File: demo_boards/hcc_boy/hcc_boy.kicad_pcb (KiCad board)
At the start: 2 copper layers, 18 x 22 mm, 24 parts, among them J2 TEST_1P, J4 TEST_1P, SW4 SW_PUSH, U1 MIC5353-3.3YMT-TR, U2 SAMD21G18, U4 SAMD21_MOD, Y1 Crystal_Small

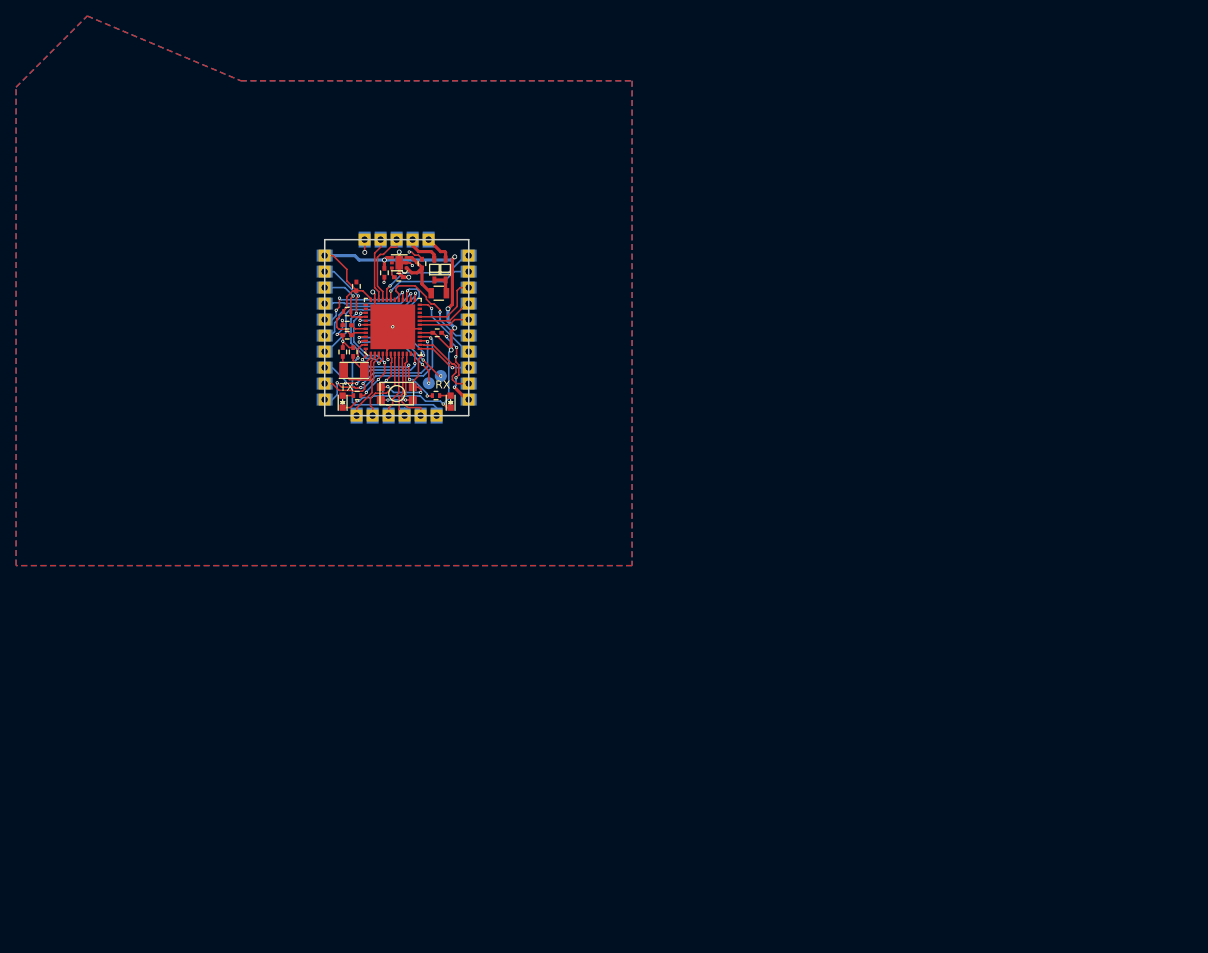
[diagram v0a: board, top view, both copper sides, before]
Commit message: added demo boards
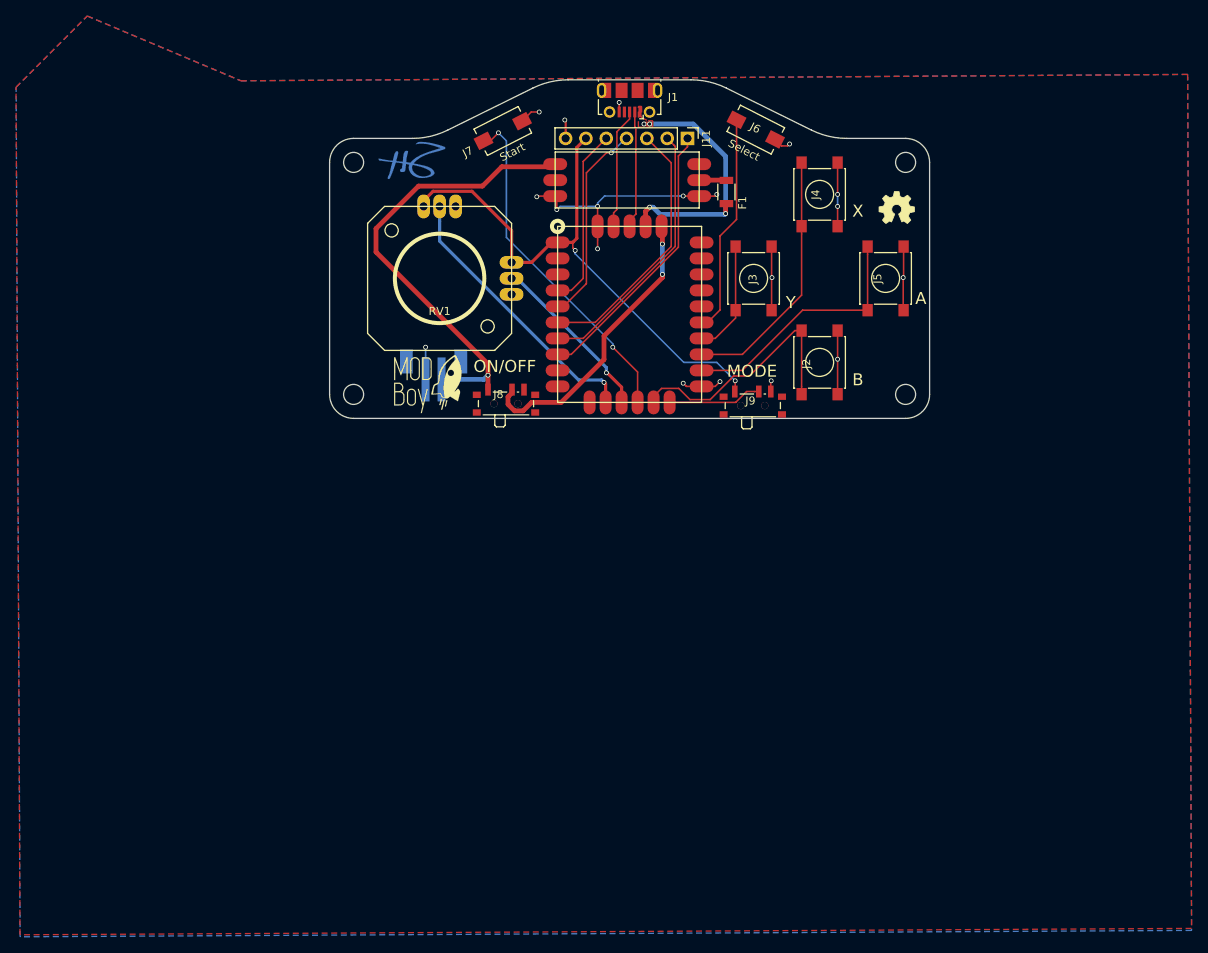
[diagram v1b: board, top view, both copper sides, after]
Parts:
- removed C11, C12, C3, C5, C6: 0.1uF, Capacitors_SMD:C_0402
- removed C2, C4: 15pF, Capacitors_SMD:C_0402
- removed C8, C9: 1uF, Capacitors_SMD:C_0402
- removed D1, D2: LED, LEDs:LED-0603
- removed D3, D4: BAT20J, agg:SOD-323
- removed R3: 10k, Resistors_SMD:R_0402
- removed R8, R9: 1k, Resistors_SMD:R_0402
- removed SW4: SW_PUSH, idlehands_footprints:switch_kmr2
- removed U2: SAMD21G18, idlehands_footprints:QFN-48-EP-ST_NoVia
- removed Y1: Crystal_Small, idlehands_footprints:crystal_smd_3.20x1.50mm2
- added BT1: Battery_Cell, Connectors_JST:JST_PH_B2B-PH-SM4-TB_02x2.00mm_Straight, B.Cu at (113.6, 94.3)
- added G***: LOGO, project_footprints:MODBoy_Logo, F.Cu at (113.0, 95.8)
- added G***: LOGO, project_footprints:MODBoy_Logo_Mask, F.Cu at (113.0, 95.8)
- added G***: LOGO, idlehands_footprints:SH_LOGO, B.Cu at (110.9, 68.2)
- added G***: LOGO, idlehands_footprints:SH_LOGOcu, B.Cu at (110.9, 68.2)
- added G***: LOGO, idlehands_footprints:OSHLogo, F.Cu at (171.5, 74.0)
- added J1: USB_OTG, Connectors_USB:USB_Micro-B_Molex-105017-0001, F.Cu at (138.1, 59.7)
- added J11: OLED, Pin_Headers:Pin_Header_Straight_1x07_Pitch2.54mm, F.Cu at (145.4, 65.3)
- added J3: B, project_footprints:SW_SPST_PTS645, F.Cu at (153.6, 82.8)
- added J5: Y, project_footprints:SW_SPST_PTS645, F.Cu at (170.1, 82.8)
- added J6: Start, Buttons_Switches_SMD:SW_SPST_EVQPE1, F.Cu at (153.9, 64.2)
- added J7: Select, Buttons_Switches_SMD:SW_SPST_EVQPE1, F.Cu at (122.3, 64.4)
- added J8: PWR, Buttons_Switches_SMD:SW_SPDT_PCM12, F.Cu at (122.7, 98.2)
- added J9: Selector, Buttons_Switches_SMD:SW_SPDT_PCM12, F.Cu at (153.5, 98.4)
- added RV1: JOYSTICK, idlehands_footprints:JOYSTICK_MINI_2AXIS, F.Cu at (114.4, 82.8)
- F1: value 500mA -> Fuse; footprint Resistors_SMD:R_0805 -> Resistors_SMD:R_1206
- J2: value TEST_1P -> A; footprint idlehands_footprints:TESTP_1_5 -> project_footprints:SW_SPST_PTS645; moved to F.Cu
- J4: value TEST_1P -> X; footprint idlehands_footprints:TESTP_1_5 -> project_footprints:SW_SPST_PTS645; moved to F.Cu
- U1: value MIC5353-3.3YMT-TR -> charge_mod; footprint agg:DFN-6-EP-ONSEMI -> idlehands_libs:LIPO_CHARGE_MOD_FOOTPRINT
- U4: footprint idlehands_footprints:SAMD21G18_MOD -> idlehands_libs:SAMD_HCC_G_FOOT
- moved J4 52.5 mm to (161.9, 72.3), turned to 90 degrees
- moved J2 48.9 mm to (161.9, 93.3), turned to 90 degrees
- moved F1 38.1 mm to (150.2, 72.0), turned to 90 degrees
- moved U1 30.3 mm to (137.8, 70.5), turned to 0 degrees
- moved U4 29.2 mm to (138.1, 87.3)
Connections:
- F1 pad 1: Net-(D3-Pad1) -> VBUS
- F1 pad 2: Net-(C8-Pad1) -> Net-(F1-Pad2)
- J2 pad 1: SWDIO -> A4
- J4 pad 1: SWCLK -> D4
- U1 pad 1: Net-(C8-Pad1) -> +BATT
- U1 pad 2: GND -> Net-(F1-Pad2)
- U1 pad 3: Net-(C8-Pad1) -> GND
- U4 pad 25: SDA -> SDI
- U4 pad 26: SCL -> CKI
- U4 pad 27: +BATT -> Net-(J8-Pad2)
- U4 pad 29: USB_D- -> Net-(J1-Pad2)
- U4 pad 30: USB_D+ -> Net-(J1-Pad3)
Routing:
- net +BATT: track 3.63 -> 57.7 mm, vias 0 -> 1
- net Net-(J8-Pad2): track 0.00 -> 36.8 mm, vias 0 -> 2
- net GND: track 48.9 -> 83.4 mm, vias 20 -> 19
- net A3: track 9.18 -> 43.2 mm, vias 0 -> 2
- net RESET: track 30.5 -> 0.00 mm, vias 5 -> 0
- net VBUS: track 4.49 -> 32.8 mm, vias 0 -> 4
- net D4: track 7.09 -> 32.1 mm, vias 1 -> 0
- net A1: track 9.90 -> 34.8 mm, vias 0 -> 1
- net D3: track 9.74 -> 31.8 mm
- net RX/D0: track 21.7 -> 0.00 mm, vias 3 -> 0
- net A4: track 10.8 -> 31.8 mm
- net D9: track 14.7 -> 34.7 mm, vias 3 -> 0
- net TX/D1: track 19.4 -> 0.00 mm, vias 2 -> 0
- net D11: track 15.5 -> 33.7 mm, vias 1 -> 0
- net AREF: track 17.7 -> 0.00 mm, vias 3 -> 0
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- added copper zone on F.Cu, net VBUS
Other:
- board size 18 x 22 mm -> 75 x 42.3 mm
- board text added: "A"
- board text added: "B"
- board text added: "MODBoy_V01p Kickstarter Demo Board for HCC MODULE YouTube.com/SeanHodginsFilms"
- board text added: "MODE"
- board text added: "ON/OFF"
- board text added: "Select"
- board text added: "Start"
- board text added: "X"
- board text added: "Y"
- board text removed: "RX"
- board text removed: "TX"
- board text removed: "bridge_mod v01p"

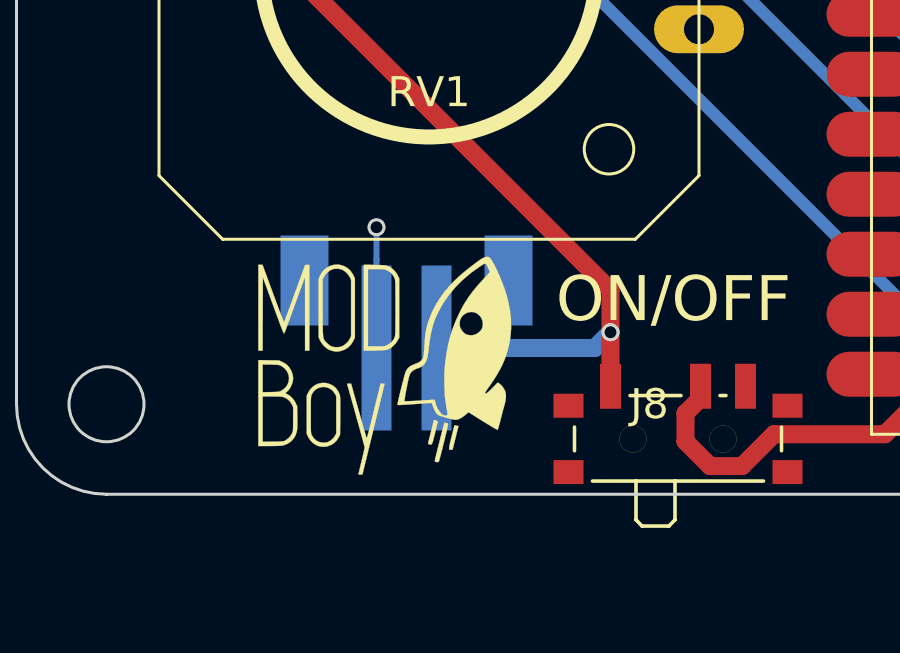
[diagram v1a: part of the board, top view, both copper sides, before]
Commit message: fixed battery connection on HCC_Boy
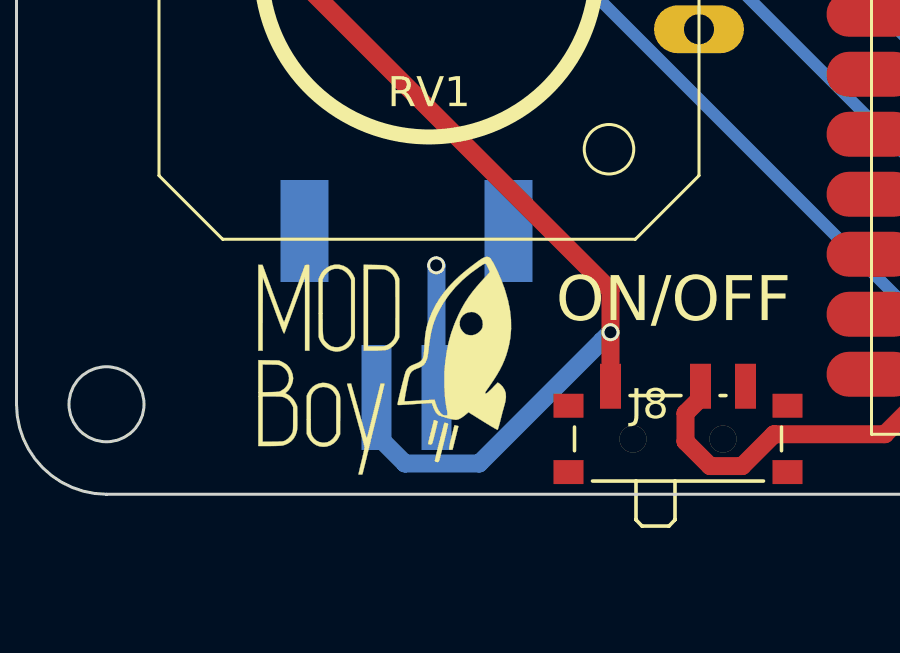
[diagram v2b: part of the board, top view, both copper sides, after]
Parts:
- BT1: footprint Connectors_JST:JST_PH_B2B-PH-SM4-TB_02x2.00mm_Straight -> Connectors_JST_PH:Connectors_JST_S2B-PH-SM4-TB
- turned BT1 to 0 degrees
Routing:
- net +BATT: track 57.7 -> 62.9 mm
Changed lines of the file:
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@@
-(kicad_pcb (version 4) (host pcbnew 4.0.4-stable)
+(kicad_pcb (version 4) (host pcbnew 4.0.7)
   (general
     (links 58)
-    (no_connects 7)
+    (no_connects 8)
     (area 61.42 50.05 208.370001 165.150001)
     (thickness 1.6)
     (drawings 36)
-    (tracks 237)
+    (tracks 240)
     (zones 0)
     (modules 20)
@@
   )
   (setup
-    (last_trace_width 0.2)
+    (last_trace_width 0.6)
     (user_trace_width 0.2)
     (user_trace_width 0.4)
@@
       (net 1 GND))
     (model ${KISYS3DMOD}/Pin_Headers.3dshapes/Pin_Header_Straight_1x07_Pitch2.54mm.wrl
-      (at (xyz 0 0 0))
-      (scale (xyz 1 1 1))
-      (rotate (xyz 0 0 0))
-    )
-  )
-  (module Connectors_JST:JST_PH_B2B-PH-SM4-TB_02x2.00mm_Straight (layer B.Cu)
-    (at 113.62 94.35 180)
-    (descr "JST PH series connector, B2B-PH-SM4-TB, top entry type, surface mount, Datasheet: http://www.jst-mfg.com/product/pdf/eng/ePH.pdf")
-    (tags "connector jst ph")
-    (attr smd)
-    (fp_text reference BT1 (at 0 4.625 180) (layer B.SilkS)
-      (effects (font (size 1 1) (thickness 0.15)) (justify mirror))
-    )
-    (fp_text value Battery_Cell (at 0 -4.875 180) (layer B.Fab)
-      (effects (font (size 1 1) (thickness 0.15)) (justify mirror))
-    )
-    (fp_line (start -4.075 2.9) (end -4.075 3.725) (layer B.SilkS) (width 0.12))
-    (fp_line (start -4.075 3.725) (end 4.075 3.725) (layer B.SilkS) (width 0.12))
-    (fp_line (start 4.075 3.725) (end 4.075 2.9) (layer B.SilkS) (width 0.12))
-    (fp_line (start -4.075 -0.65) (end -4.075 -1.475) (layer B.SilkS) (width 0.12))
-    (fp_line (start -4.075 -1.475) (end -1.775 -1.475) (layer B.SilkS) (width 0.12))
-    (fp_line (start 4.075 -0.65) (end 4.075 -1.475) (layer B.SilkS) (width 0.12))
-    (fp_line (start 4.075 -1.475) (end 1.775 -1.475) (layer B.SilkS) (width 0.12))
-    (fp_line (start -3.975 3.625) (end -3.975 -1.375) (layer B.Fab) (width 0.1))
-    (fp_line (start -3.975 -1.375) (end 3.975 -1.375) (layer B.Fab) (width 0.1))
-    (fp_line (start 3.975 -1.375) (end 3.975 3.625) (layer B.Fab) (width 0.1))
-    (fp_line (start 3.975 3.625) (end -3.975 3.625) (layer B.Fab) (width 0.1))
-    (fp_line (start -1.775 -1.475) (end -1.775 -3.875) (layer B.SilkS) (width 0.12))
-    (fp_line (start -2 -1.375) (end -1 -0.375) (layer B.Fab) (width 0.1))
-    (fp_line (start -1 -0.375) (end 0 -1.375) (layer B.Fab) (width 0.1))
-    (fp_line (start -4.7 4.13) (end -4.7 -4.38) (layer B.CrtYd) (width 0.05))
-    (fp_line (start -4.7 -4.38) (end 4.7 -4.38) (layer B.CrtYd) (width 0.05))
-    (fp_line (start 4.7 -4.38) (end 4.7 4.13) (layer B.CrtYd) (width 0.05))
-    (fp_line (start 4.7 4.13) (end -4.7 4.13) (layer B.CrtYd) (width 0.05))
-    (fp_text user %R (at 0 2.625 180) (layer B.Fab)
-      (effects (font (size 1 1) (thickness 0.15)) (justify mirror))
-    )
-    (pad 1 smd rect (at -1 -1.125 180) (size 1 5.5) (layers B.Cu B.Paste B.Mask)
-      (net 25 +BATT))
-    (pad 2 smd rect (at 1 -1.125 180) (size 1 5.5) (layers B.Cu B.Paste B.Mask)
-      (net 1 GND))
-    (pad "" smd rect (at -3.4 1.125 180) (size 1.6 3) (layers B.Cu B.Paste B.Mask))
-    (pad "" smd rect (at 3.4 1.125 180) (size 1.6 3) (layers B.Cu B.Paste B.Mask))
-    (model ${KISYS3DMOD}/Connectors_JST.3dshapes/JST_PH_B2B-PH-SM4-TB_02x2.00mm_Straight.wrl
       (at (xyz 0 0 0))
       (scale (xyz 1 1 1))
@@
       (xy 2.197782 0.021915) (xy 2.199387 0.08875) (xy 2.199993 0.164819) (xy 2.199993 0.164819)) (layer F.SilkS) (width 0.1))
   )
+  (module Connectors_JST_PH:Connectors_JST_S2B-PH-SM4-TB (layer B.Cu)
+    (at 113.62 94.35)
+    (descr "JST PH series connector, S2B-PH-SM4-TB")
+    (tags "connector jst ph")
+    (attr smd)
+    (fp_text reference BT1 (at -1 5.775) (layer B.SilkS)
+      (effects (font (size 1 1) (thickness 0.15)) (justify mirror))
+    )
+    (fp_text value Battery_Cell (at 0 -5.725) (layer B.Fab)
+      (effects (font (size 1 1) (thickness 0.15)) (justify mirror))
+    )
+    (fp_circle (center -2.4 2.525) (end -2.15 2.525) (layer B.SilkS) (width 0.15))
+    (fp_line (start -0.5 -4.225) (end -0.5 -3.225) (layer B.SilkS) (width 0.15))
+    (fp_line (start -0.5 -3.225) (end 0.5 -3.225) (layer B.SilkS) (width 0.15))
+    (fp_line (start 0.5 -3.225) (end 0.5 -4.225) (layer B.SilkS) (width 0.15))
+    (fp_line (start -1.9 1.775) (end -3.15 1.775) (layer B.SilkS) (width 0.15))
+    (fp_line (start -3.15 1.775) (end -3.15 3.375) (layer B.SilkS) (width 0.15))
+    (fp_line (start -3.15 3.375) (end -3.95 3.375) (layer B.SilkS) (width 0.15))
+    (fp_line (start -3.95 3.375) (end -3.95 -0.725) (layer B.SilkS) (width 0.15))
+    (fp_line (start -3.15 1.775) (end -3.95 1.775) (layer B.SilkS) (width 0.15))
+    (fp_line (start 1.9 1.775) (end 3.15 1.775) (layer B.SilkS) (width 0.15))
+    (fp_line (start 3.15 1.775) (end 3.15 3.375) (layer B.SilkS) (width 0.15))
+    (fp_line (start 3.15 3.375) (end 3.95 3.375) (layer B.SilkS) (width 0.15))
+    (fp_line (start 3.95 3.375) (end 3.95 -0.725) (layer B.SilkS) (width 0.15))
+    (fp_line (start 3.15 1.775) (end 3.95 1.775) (layer B.SilkS) (width 0.15))
+    (fp_line (start -2.2 -4.225) (end 2.2 -4.225) (layer B.SilkS) (width 0.15))
+    (fp_line (start -2.2 0.675) (end -2.2 -2.725) (layer B.SilkS) (width 0.15))
+    (fp_line (start -2.2 -2.725) (end -1.2 -2.725) (layer B.SilkS) (width 0.15))
+    (fp_line (start -1.2 -2.725) (end -1.2 0.675) (layer B.SilkS) (width 0.15))
+    (fp_line (start -1.2 0.675) (end -2.2 0.675) (layer B.SilkS) (width 0.15))
+    (fp_line (start 2.2 0.675) (end 2.2 -2.725) (layer B.SilkS) (width 0.15))
+    (fp_line (start 2.2 -2.725) (end 1.2 -2.725) (layer B.SilkS) (width 0.15))
+    (fp_line (start 1.2 -2.725) (end 1.2 0.675) (layer B.SilkS) (width 0.15))
+    (fp_line (start 1.2 0.675) (end 2.2 0.675) (layer B.SilkS) (width 0.15))
+    (fp_line (start -0.1 1.775) (end 0.1 1.775) (layer B.SilkS) (width 0.15))
+    (fp_line (start -4.7 -5) (end -4.7 5.05) (layer B.CrtYd) (width 0.05))
+    (fp_line (start -4.7 5.05) (end 4.7 5.05) (layer B.CrtYd) (width 0.05))
+    (fp_line (start 4.7 5.05) (end 4.7 -5) (layer B.CrtYd) (width 0.05))
+    (fp_line (start 4.7 -5) (end -4.7 -5) (layer B.CrtYd) (width 0.05))
+    (pad 1 smd rect (at -1 2.775) (size 1 3.5) (layers B.Cu B.Paste B.Mask)
+      (net 25 +BATT))
+    (pad 2 smd rect (at 1 2.775) (size 1 3.5) (layers B.Cu B.Paste B.Mask)
+      (net 1 GND))
+    (pad "" smd rect (at -3.4 -2.775) (size 1.6 3.4) (layers B.Cu B.Paste B.Mask))
+    (pad "" smd rect (at 3.4 -2.775) (size 1.6 3.4) (layers B.Cu B.Paste B.Mask))
+  )
   (dimension 42.5 (width 0.3) (layer Cmts.User)
     (gr_text "42.500 mm" (at 79.27 79.1 90) (layer Cmts.User)
@@
   (gr_arc (start 103.62 97.35) (end 100.62 97.35) (angle -89.999992) (layer Edge.Cuts) (width 0.1))
   (gr_line (start 100.62 97.35) (end 100.62 68.35) (layer Edge.Cuts) (width 0.1))
+  (segment (start 114.62 97.125) (end 114.62 92.73) (width 0.6) (layer B.Cu) (net 1))
+  (segment (start 114.62 92.73) (end 114.61 92.72) (width 0.6) (layer B.Cu) (net 1))
+  (via (at 114.61 92.72) (size 0.6) (drill 0.4) (layers F.Cu B.Cu) (net 1))
   (segment (start 134.12 73.85) (end 134.12 73.425736) (width 0.2) (layer B.Cu) (net 1))
   (segment (start 134.12 73.425736) (end 134.995736 72.55) (width 0.2) (layer B.Cu) (net 1))
@@
   (segment (start 125.824944 62.05) (end 126.82 62.05) (width 0.2) (layer F.Cu) (net 1))
   (via (at 126.82 62.05) (size 0.6) (drill 0.4) (layers F.Cu B.Cu) (net 1))
-  (segment (start 112.62 95.475) (end 112.62 92.525) (width 0.2) (layer B.Cu) (net 1))
-  (segment (start 112.62 92.525) (end 112.62 91.45) (width 0.2) (layer B.Cu) (net 1))
-  (via (at 112.62 91.45) (size 0.6) (drill 0.4) (layers F.Cu B.Cu) (net 1))
   (segment (start 155.77 96.99) (end 155.77 95.7) (width 0.2) (layer F.Cu) (net 1))
   (segment (start 155.77 95.7) (end 155.82 95.65) (width 0.2) (layer F.Cu) (net 1))
@@
   (segment (start 137.72 65.15) (end 137.9 65.15) (width 0.2) (layer B.Cu) (net 24))
   (segment (start 129.12 86.35) (end 129.87 86.35) (width 0.2) (layer F.Cu) (net 24))
+  (segment (start 112.62 97.125) (end 112.62 98.375) (width 0.6) (layer B.Cu) (net 25))
+  (segment (start 112.62 98.375) (end 113.570001 99.325001) (width 0.6) (layer B.Cu) (net 25))
+  (segment (start 113.570001 99.325001) (end 116.044999 99.325001) (width 0.6) (layer B.Cu) (net 25))
+  (segment (start 116.044999 99.325001) (end 120.120001 95.249999) (width 0.6) (layer B.Cu) (net 25))
+  (segment (start 120.120001 95.249999) (end 120.42 94.95) (width 0.6) (layer B.Cu) (net 25))
   (segment (start 120.42 94.95) (end 120.42 93.55) (width 0.6) (layer F.Cu) (net 25))
   (segment (start 120.42 93.55) (end 106.42 79.55) (width 0.6) (layer F.Cu) (net 25))
@@
   (segment (start 128.490163 68.895837) (end 128.82 68.566) (width 0.6) (layer F.Cu) (net 25))
   (segment (start 120.42 94.95) (end 120.42 96.75) (width 0.6) (layer F.Cu) (net 25))
-  (segment (start 114.62 95.475) (end 119.895 95.475) (width 0.6) (layer B.Cu) (net 25))
-  (segment (start 119.895 95.475) (end 120.42 94.95) (width 0.6) (layer B.Cu) (net 25))
   (via (at 120.42 94.95) (size 0.6) (drill 0.4) (layers F.Cu B.Cu) (net 25))
   (segment (start 140.62 63.55) (end 139.92 63.55) (width 0.6) (layer F.Cu) (net 26))
